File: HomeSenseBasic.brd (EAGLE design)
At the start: 44 x 44 mm, 21 parts, among them IC1 ESP12SMT, IC3 MS563702BA03, IC4 DHT12

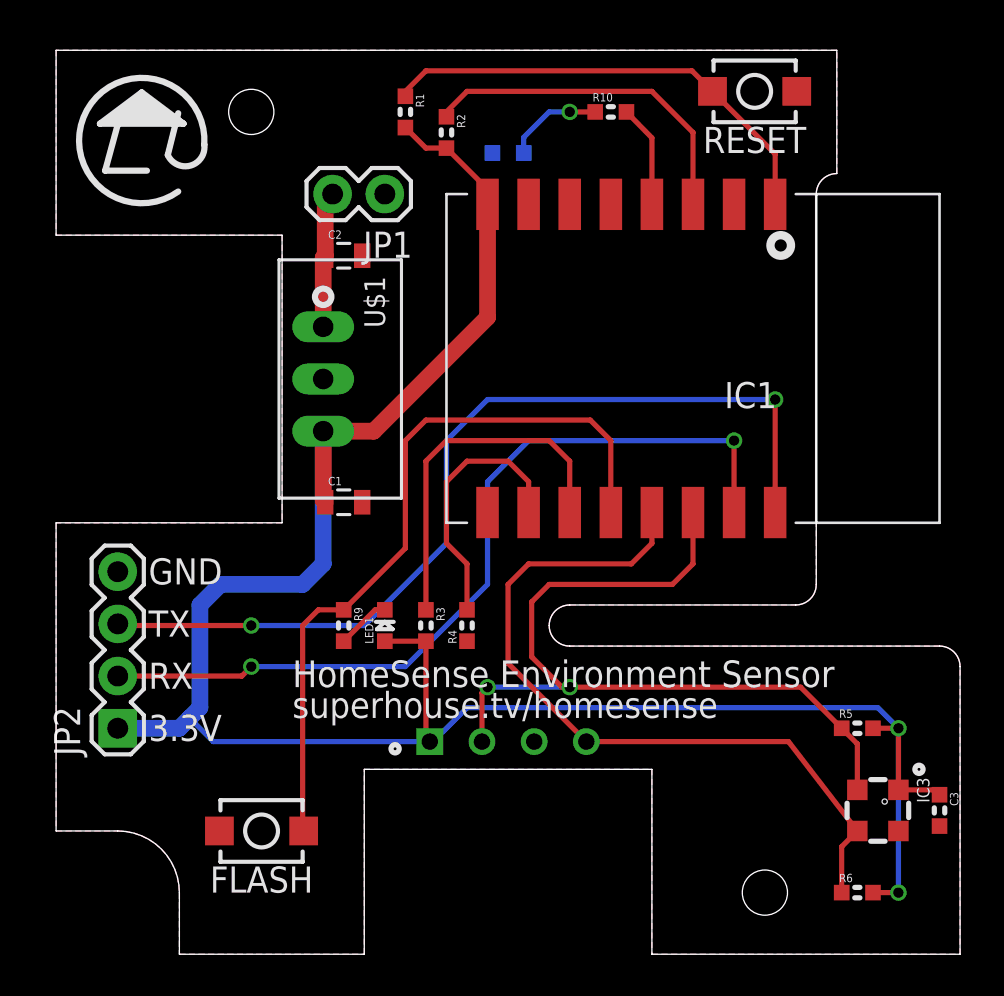
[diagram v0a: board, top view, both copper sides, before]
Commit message: Updated routing and schematic for v1.0 release
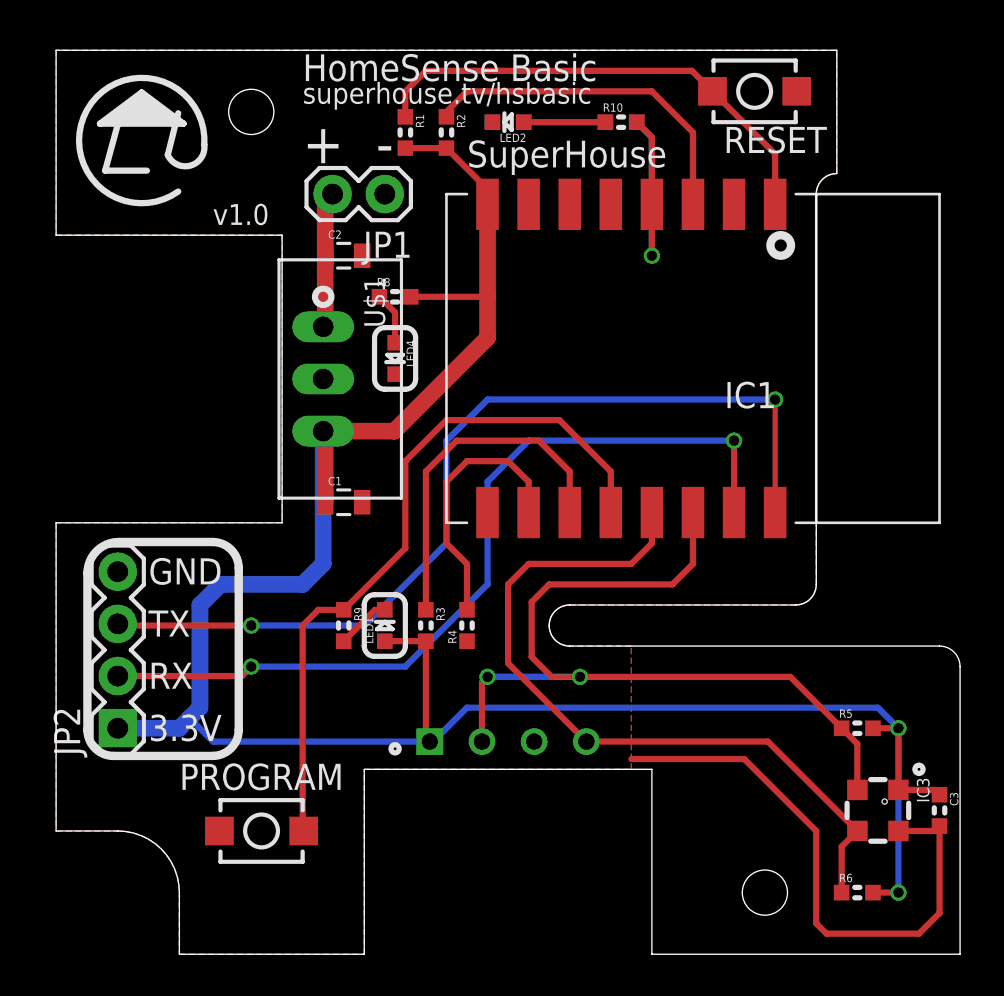
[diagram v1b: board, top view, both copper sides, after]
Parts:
- added LED3: GREEN, freetronics-jon:LED-0603
- added LED4: BLUE, freetronics-jon:LED-0603
- added R7: 1K, freetronics-jon:0603
- added R8: 4K7, freetronics-jon:0603
- S2: value FLASH -> PROGRAM
- moved LED2 1.50 mm to (22.0, 40.5), flipped to the top, turned to 180 degrees
- moved R1 1.00 mm to (17.0, 40.0)
- moved R10 0.71 mm to (27.5, 40.5)
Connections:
- new net N$11: LED3.A, R7.1
- new net N$2: LED4.A, R8.1
- net 3.3V: now also R8.2
- net GND: now also LED3.C, LED4.C
- net GPIO16: now also R7.2
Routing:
- net GND: track 0.00 -> 27.9 mm
- net GPIO16: track 5.01 -> 13.6 mm, vias 0 -> 1
- net N$11: track 0.00 -> 3.98 mm
- net 3.3V: track 106.6 -> 110.5 mm
- net N$2: track 0.00 -> 2.55 mm
- net GPIO0: track 36.1 -> 34.7 mm
- net SDA: track 40.4 -> 41.4 mm
- net RESET: track 22.8 -> 23.8 mm
- net N$4: track 4.75 -> 3.98 mm, vias 1 -> 0
- net GPIO2: track 17.6 -> 17.0 mm
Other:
- board text added: "HomeSense Basic"
- board text added: "IN"
- board text added: "OUT"
- board text added: "PROGRAM"
- board text added: "SuperHouse"
- board text added: "superhouse.tv/hsbasic"
- board text added: "v1.0"
- board text added: "www.superhouse.tv/hsbasic"
- board text removed: "FLASH"
- board text removed: "HomeSense Environment Sensor"
- board text removed: "HomeSense Environmental Sensor"
- board text removed: "superhouse.tv/homesense"
- board text removed: "www.superhouse.tv/homesense"

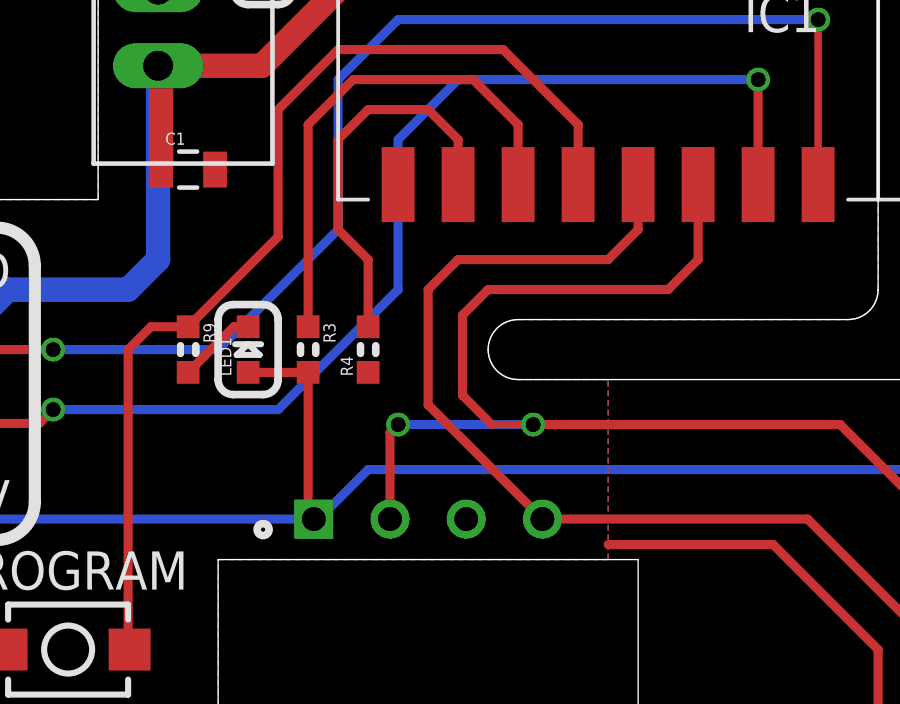
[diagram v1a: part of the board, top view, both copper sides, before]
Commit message: Fixed ESP12 footprint with correct GPIO4/5
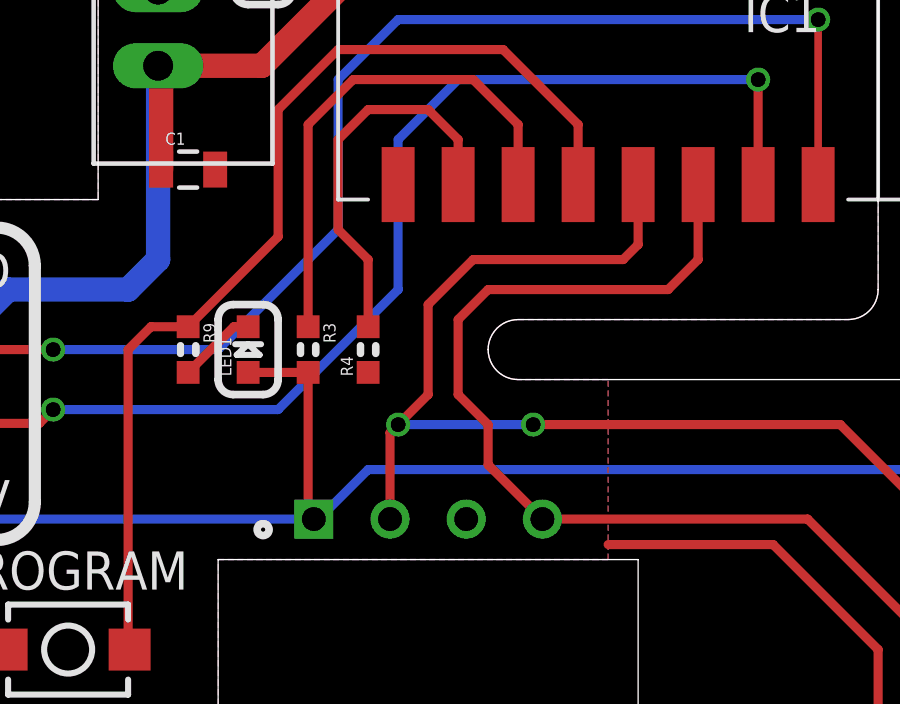
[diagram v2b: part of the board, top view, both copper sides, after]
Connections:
- net SCL: now also IC1.14; no longer IC1.13
- net SDA: now also IC1.13; no longer IC1.14
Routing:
- net SDA: track 41.4 -> 39.1 mm
- net SCL: track 36.9 -> 37.4 mm
